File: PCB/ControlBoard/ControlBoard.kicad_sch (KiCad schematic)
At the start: 51 parts, among them J1 SWD, J2 USB, J3 Bus, J4 Submodule A, J5 Submodule B, J6 Submodule C, SW1 Boot, U1 STM32H562VGT6, U2 MCP2562-E-SN, U3 TPD2E2U06DCK, U7 CM1293A‐04SO, Y1 XO22C3EREHX50M000

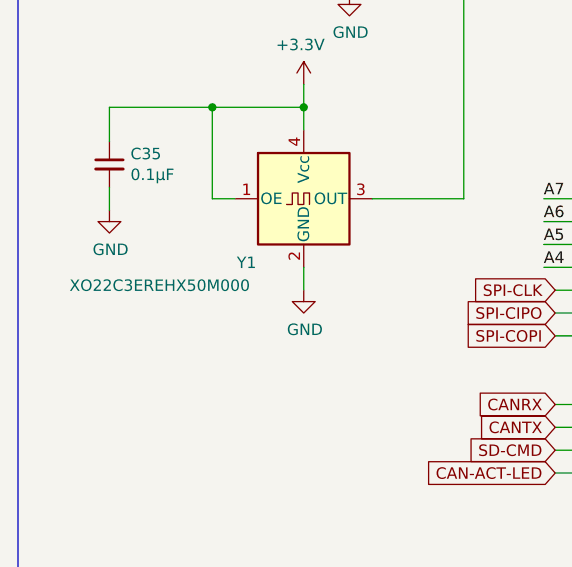
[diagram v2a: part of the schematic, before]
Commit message: fix: Change oscillator to 25Mhz, enables PLL to operate in nicer ranges.
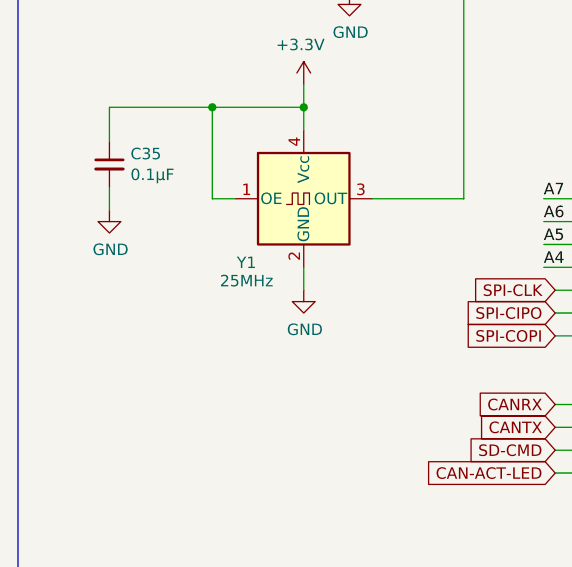
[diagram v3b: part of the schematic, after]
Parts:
- Y1: value XO22C3EREHX50M000 -> 25MHz; DIGIKEY 541-XO22C3EREHX50M000CT-ND -> 541-XO22C3EREHX25M000CT-ND
